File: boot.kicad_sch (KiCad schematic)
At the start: 7 parts, among them SW1 CAS-220TA, U1 MX6UL-VM

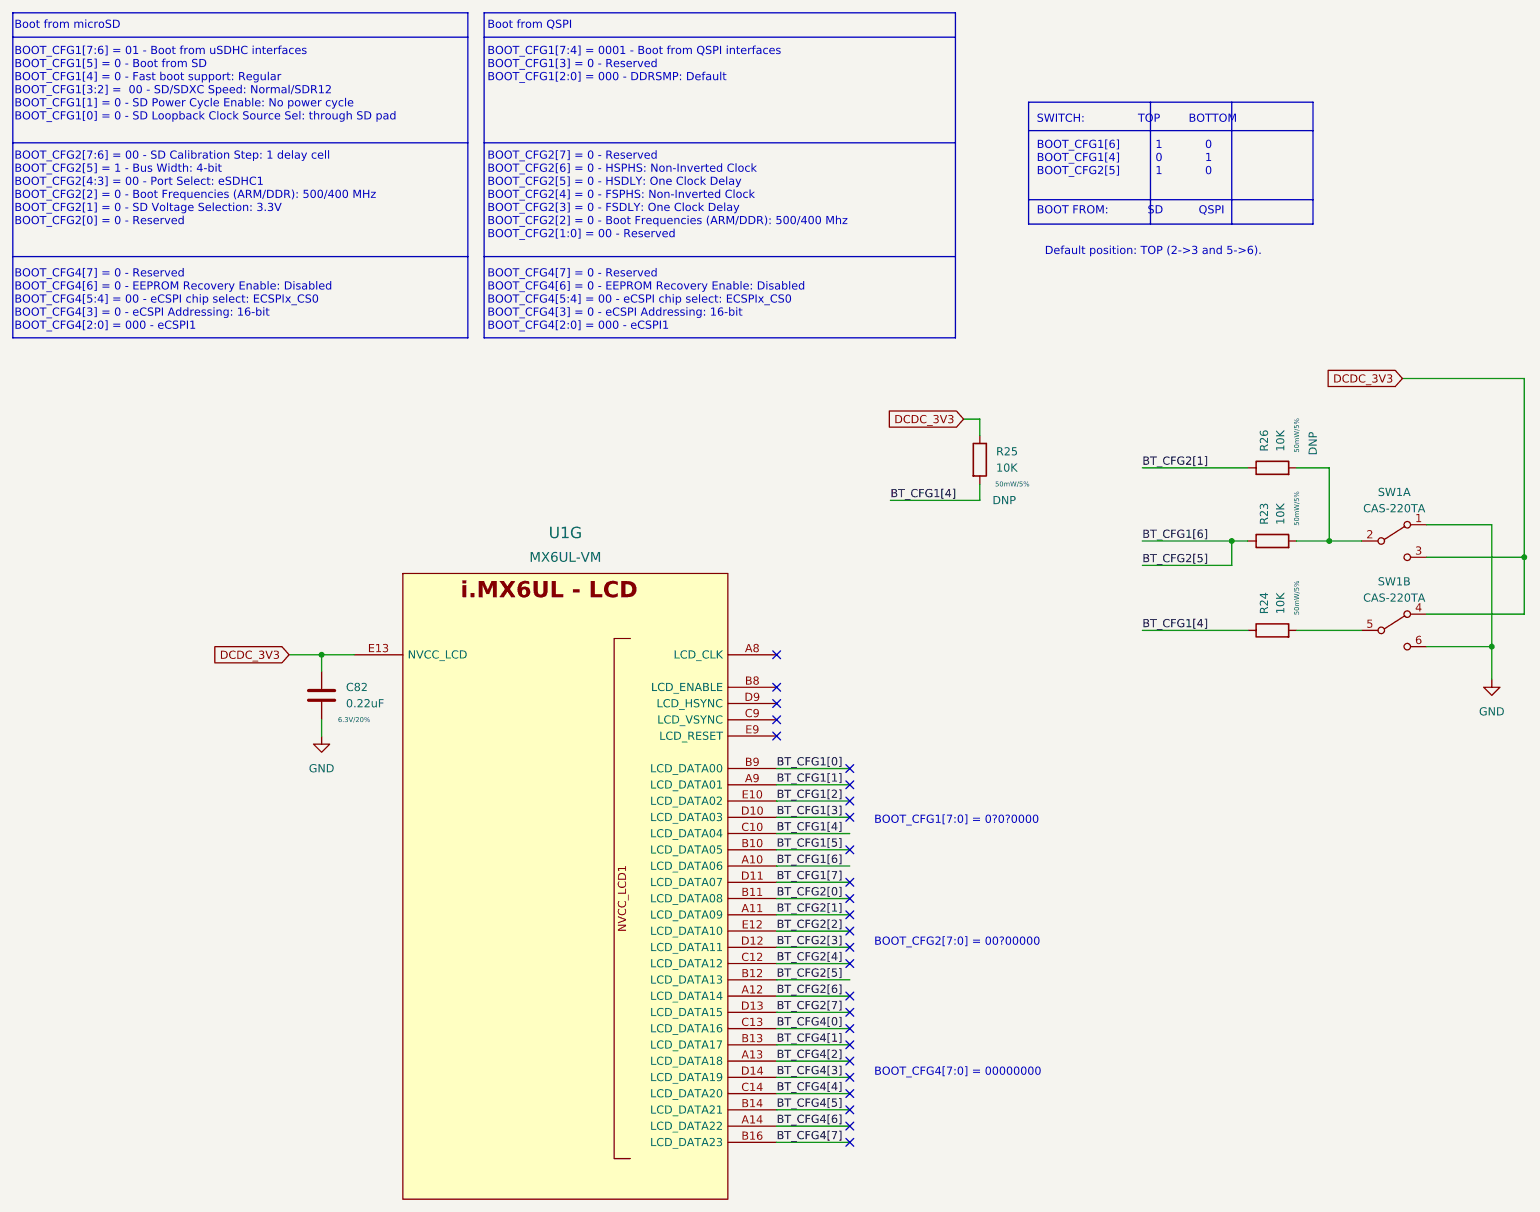
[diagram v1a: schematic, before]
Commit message: start moving to hierarchal labels, add emmc
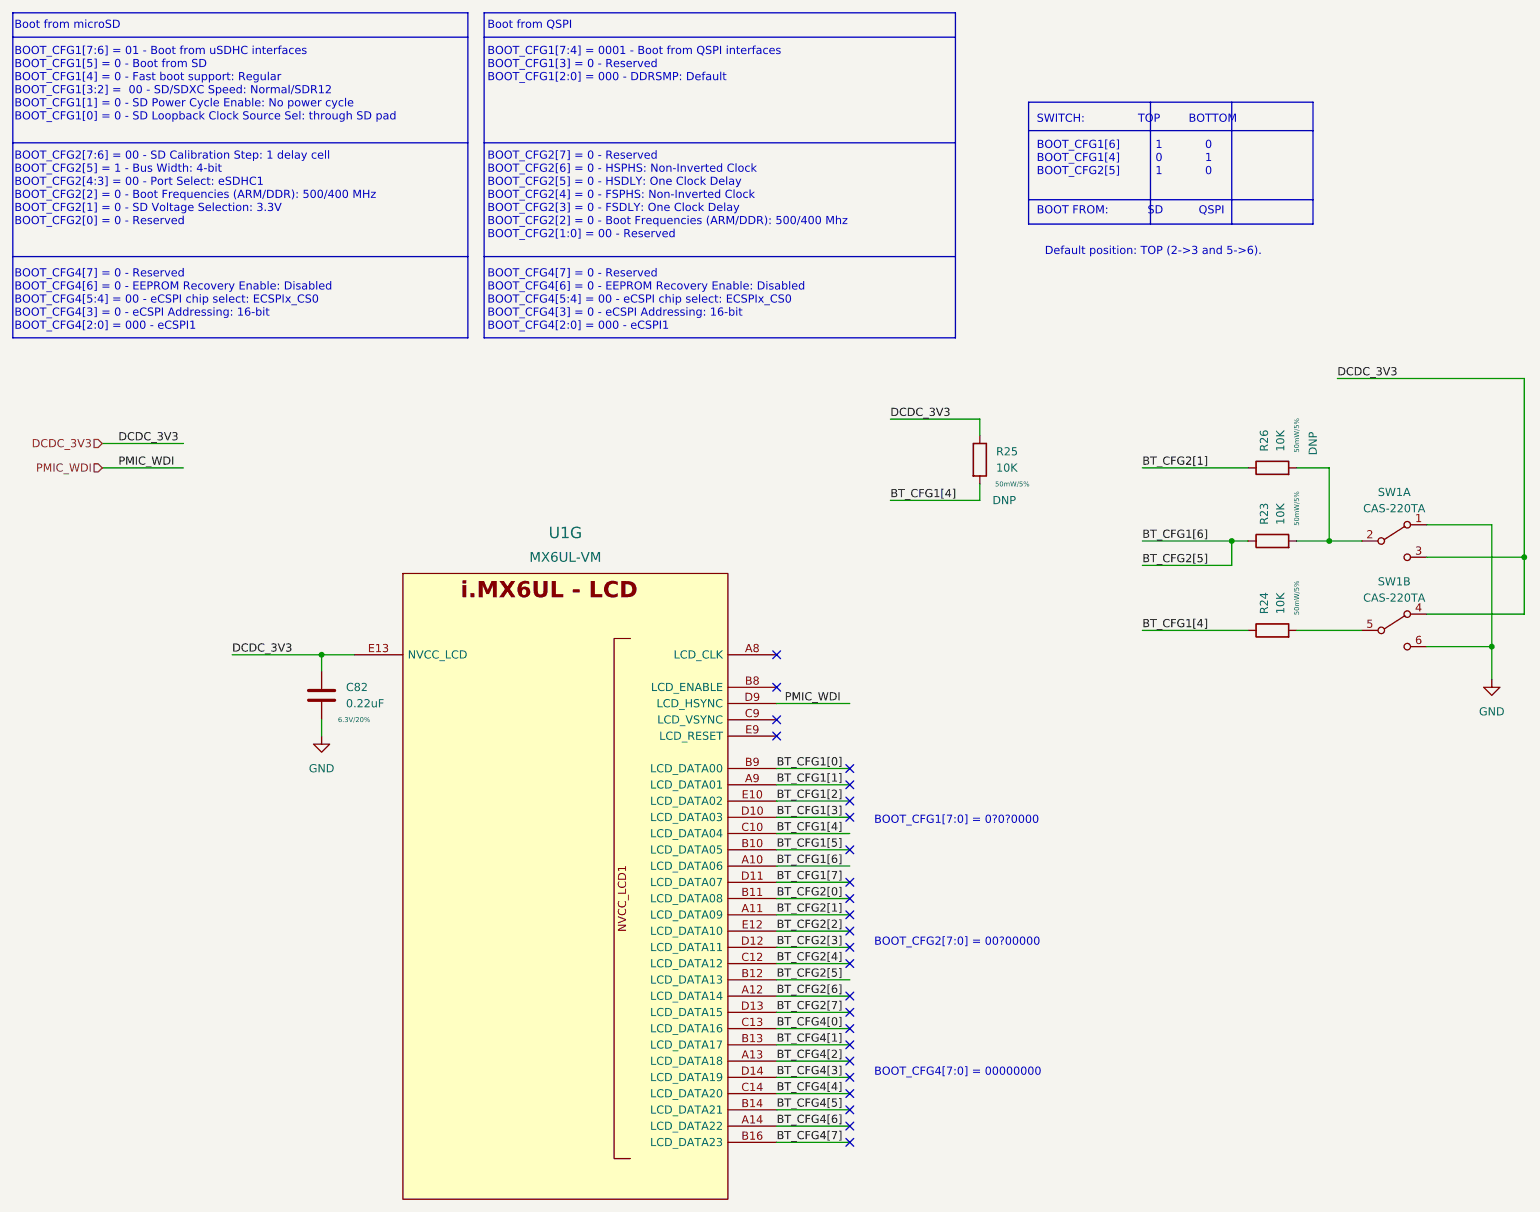
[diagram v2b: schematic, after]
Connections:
- net PMIC_WDI: now reaches U1.D9 (LCD_HSYNC)
- no-connect marks 26 -> 25
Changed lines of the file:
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@@
   (no_connect (at 144.78 157.48))
   (no_connect (at 144.78 149.86))
-  (no_connect (at 133.35 121.92))
   (no_connect (at 133.35 119.38))
   (no_connect (at 133.35 114.3))
@@
     (stroke (width 0) (type default) (color 0 0 0 0))
   )
-  (wire (pts (xy 57.15 114.3) (xy 62.23 114.3))
+  (wire (pts (xy 48.26 114.3) (xy 62.23 114.3))
     (stroke (width 0) (type default) (color 0 0 0 0))
   )
@@
     (stroke (width 0) (type default) (color 0 0 0 0))
   )
+  (wire (pts (xy 27.94 81.28) (xy 40.64 81.28))
+    (stroke (width 0) (type default) (color 0 0 0 0))
+  )
   (wire (pts (xy 133.35 187.96) (xy 144.78 187.96))
     (stroke (width 0) (type default) (color 0 0 0 0))
@@
     (stroke (width 0) (type default) (color 0 0 0 0))
   )
-  (wire (pts (xy 165.1 77.47) (xy 162.56 77.47))
+  (wire (pts (xy 151.13 77.47) (xy 165.1 77.47))
     (stroke (width 0) (type default) (color 0 0 0 0))
   )
@@
     (stroke (width 0) (type default) (color 0 0 0 0))
   )
+  (wire (pts (xy 27.94 85.09) (xy 40.64 85.09))
+    (stroke (width 0) (type default) (color 0 0 0 0))
+  )
   (wire (pts (xy 133.35 185.42) (xy 144.78 185.42))
     (stroke (width 0) (type default) (color 0 0 0 0))
@@
     (stroke (width 0) (type default) (color 0 0 0 0))
   )
+  (wire (pts (xy 133.35 121.92) (xy 144.78 121.92))
+    (stroke (width 0) (type default) (color 0 0 0 0))
+  )
   (wire (pts (xy 133.35 132.08) (xy 144.78 132.08))
     (stroke (width 0) (type default) (color 0 0 0 0))
@@
     (stroke (width 0) (type default) (color 0 0 0 0))
   )
-  (wire (pts (xy 231.14 71.12) (xy 250.19 71.12))
+  (wire (pts (xy 220.98 71.12) (xy 250.19 71.12))
     (stroke (width 0) (type default) (color 0 0 0 0))
   )
@@
     (effects (font (size 1.27 1.27)) (justify left bottom))
   )
+  (label "DCDC_3V3" (at 48.26 114.3 0)
+    (effects (font (size 1.27 1.27)) (justify left bottom))
+  )
   (label "BT_CFG2[3]" (at 133.35 160.02 0)
     (effects (font (size 1.27 1.27)) (justify left bottom))
@@
     (effects (font (size 1.27 1.27)) (justify left bottom))
   )
+  (label "DCDC_3V3" (at 151.13 77.47 0)
+    (effects (font (size 1.27 1.27)) (justify left bottom))
+  )
   (label "BT_CFG1[4]" (at 151.13 90.17 0)
     (effects (font (size 1.27 1.27)) (justify left bottom))
@@
     (effects (font (size 1.27 1.27)) (justify left bottom))
   )
+  (label "PMIC_WDI" (at 134.62 121.92 0)
+    (effects (font (size 1.27 1.27)) (justify left bottom))
+  )
   (label "BT_CFG2[0]" (at 133.35 152.4 0)
     (effects (font (size 1.27 1.27)) (justify left bottom))
@@
     (effects (font (size 1.27 1.27)) (justify left bottom))
   )
+  (label "DCDC_3V3" (at 30.48 81.28 0)
+    (effects (font (size 1.27 1.27)) (justify left bottom))
+  )
   (label "BT_CFG4[3]" (at 133.35 180.34 0)
     (effects (font (size 1.27 1.27)) (justify left bottom))
@@
     (effects (font (size 1.27 1.27)) (justify left bottom))
   )
+  (label "DCDC_3V3" (at 220.98 71.12 0)
+    (effects (font (size 1.27 1.27)) (justify left bottom))
+  )
   (label "BT_CFG2[1]" (at 190.5 85.09 0)
     (effects (font (size 1.27 1.27)) (justify left bottom))
@@
     (effects (font (size 1.27 1.27)) (justify left bottom))
   )
+  (label "PMIC_WDI" (at 30.48 85.09 0)
+    (effects (font (size 1.27 1.27)) (justify left bottom))
+  )
   (label "BT_CFG4[1]" (at 133.35 175.26 0)
     (effects (font (size 1.27 1.27)) (justify left bottom))
@@
     (effects (font (size 1.27 1.27)) (justify left bottom))
   )
-  (global_label "DCDC_3V3" (shape input) (at 162.56 77.47 180) (fields_autoplaced)
+  (hierarchical_label "PMIC_WDI" (shape input) (at 27.94 85.09 180)
     (effects (font (size 1.27 1.27)) (justify right))
-    (property "Intersheet References" "${INTERSHEET_REFS}" (id 0) (at 150.5917 77.5494 0)
-      (effects (font (size 1.27 1.27)) (justify right) hide)
-    )
-  )
-  (global_label "DCDC_3V3" (shape input) (at 57.15 114.3 180) (fields_autoplaced)
+  )
+  (hierarchical_label "DCDC_3V3" (shape input) (at 27.94 81.28 180)
     (effects (font (size 1.27 1.27)) (justify right))
-    (property "Intersheet References" "${INTERSHEET_REFS}" (id 0) (at 45.1817 114.3794 0)
-      (effects (font (size 1.27 1.27)) (justify right) hide)
-    )
-  )
-  (global_label "DCDC_3V3" (shape input) (at 231.14 71.12 180) (fields_autoplaced)
-    (effects (font (size 1.27 1.27)) (justify right))
-    (property "Intersheet References" "${INTERSHEET_REFS}" (id 0) (at 219.1717 71.1994 0)
-      (effects (font (size 1.27 1.27)) (justify right) hide)
-    )
   )
   (symbol (lib_id "power:GND") (at 62.23 127 0) (unit 1)

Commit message: lots of routing, ddr length matching done
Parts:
- SW1: footprint imx6ull-sbc:CAS-220-A -> qsbc-zero:CAS-220-A
- U1: footprint imx6ull-sbc:SOT1534-2 -> qsbc-zero:SOT1534-2; symbol imx6ull-sbc:MX6UL-VM -> qsbc-zero:MX6UL-VM
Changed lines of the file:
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@@
     (property "Reference" "SW1" (id 0) (at 229.87 102.87 0))
     (property "Value" "CAS-220TA" (id 1) (at 229.87 105.41 0))
-    (property "Footprint" "imx6ull-sbc:CAS-220-A" (id 2) (at 229.87 110.49 0)
+    (property "Footprint" "qsbc-zero:CAS-220-A" (id 2) (at 229.87 110.49 0)
       (effects (font (size 1.27 1.27)) hide)
     )
@@
     (pin "2")
   )
-  (symbol (lib_id "imx6ull-sbc:MX6UL-VM") (at 100.33 101.6 0) (unit 7)
+  (symbol (lib_id "qsbc-zero:MX6UL-VM") (at 100.33 101.6 0) (unit 7)
     (in_bom yes) (on_board yes) (fields_autoplaced)
     (property "Reference" "U1" (id 0) (at 100.33 95.25 0)
@@
       (effects (font (size 1.524 1.524)))
     )
-    (property "Footprint" "imx6ull-sbc:SOT1534-2" (id 2) (at 113.284 131.064 0)
+    (property "Footprint" "qsbc-zero:SOT1534-2" (id 2) (at 113.284 131.064 0)
       (effects (font (size 1.524 1.524)) hide)
     )
@@
     (property "Reference" "SW1" (id 0) (at 229.87 88.9 0))
     (property "Value" "CAS-220TA" (id 1) (at 229.87 91.44 0))
-    (property "Footprint" "imx6ull-sbc:CAS-220-A" (id 2) (at 229.87 96.52 0)
+    (property "Footprint" "qsbc-zero:CAS-220-A" (id 2) (at 229.87 96.52 0)
       (effects (font (size 1.27 1.27)) hide)
     )
